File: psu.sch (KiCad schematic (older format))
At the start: 1 part

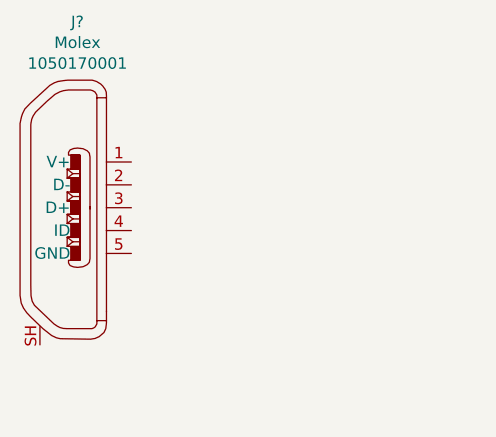
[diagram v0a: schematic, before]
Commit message: Add ESD protection to USB
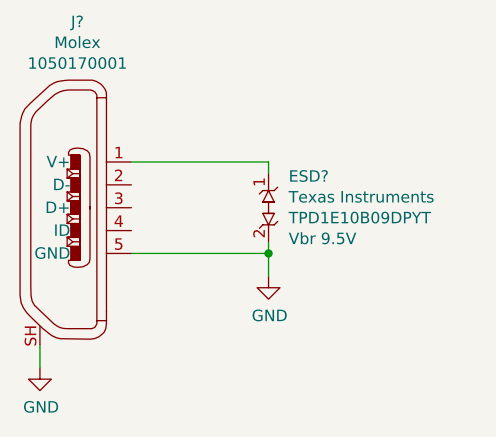
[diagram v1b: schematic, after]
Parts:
- added ESD?: TI-TPD1E10B09DPYT, footprints:TI-TPD1E10B09DPYT_DIODFN2_100X60X45L25X50N, symbol gz_TVS-Diodes:TI-TPD1E10B09DPYT
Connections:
- net at J?.1 (V+): now also ESD?.1
- net GND: now reaches J?.5 (GND)
- net GND: now also J?.SH, ESD?.2
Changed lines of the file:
@@
 	1    0    0    -1
 $EndComp
+$Comp
+L gz_TVS-Diodes:TI-TPD1E10B09DPYT ESD?
+U 1 1 60436474
+P 2350 1900
+F 0 "ESD?" H 2438 2037 50  0000 L CNN
+F 1 "TI-TPD1E10B09DPYT" H 3150 2900 50  0001 L CNN
+F 2 "footprints:TI-TPD1E10B09DPYT_DIODFN2_100X60X45L25X50N" H 3150 2800 50  0001 L CNN
+F 3 "${DATASHEETS}/TI-TPD1E10B09DPYT.pdf" H 2550 2200 50  0001 L CNN
+F 4 "Digikey" H 3150 2700 50  0001 L CNN "Vendor"
+F 5 "296-46461-1-ND" H 3550 2700 50  0001 L CNN "Vendor_PN"
+F 6 "Texas Instruments" H 2438 1946 50  0000 L CNN "Manufacturer"
+F 7 "TPD1E10B09DPYT" H 2438 1855 50  0000 L CNN "MPN"
+F 8 "Circuit protection" H 3150 2600 50  0001 L CNN "Category"
+F 9 "TVS - Diodes" H 3150 2500 50  0001 L CNN "Family"
+F 10 "Y" H 2800 2050 50  0001 L CNN "Fit"
+F 11 "Vbr 9.5V" H 2438 1764 50  0000 L CNN "Breakdown Voltage"
+F 12 "EIA0402" H 3150 2400 50  0001 L CNN "Package"
+	1    2350 1900
+	1    0    0    -1
+$EndComp
+Wire Wire Line
+	1750 1700 2350 1700
+Wire Wire Line
+	2350 1700 2350 1750
+Wire Wire Line
+	2350 2050 2350 2100
+$Comp
+L gz_Power-Symbols:GND #PWR?
+U 1 1 60439CF7
+P 2350 2200
+F 0 "#PWR?" H 2350 1950 50  0001 C CNN
+F 1 "GND" H 2355 2027 50  0000 C CNN
+F 2 "" H 2350 2200 50  0001 C CNN
+F 3 "" H 2350 2200 50  0001 C CNN
+	1    2350 2200
+	1    0    0    -1
+$EndComp
+Wire Wire Line
+	1750 2100 2350 2100
+Connection ~ 2350 2100
+Wire Wire Line
+	2350 2100 2350 2200
+$Comp
+L gz_Power-Symbols:GND #PWR?
+U 1 1 6043BB02
+P 1350 2600
+F 0 "#PWR?" H 1350 2350 50  0001 C CNN
+F 1 "GND" H 1355 2427 50  0000 C CNN
+F 2 "" H 1350 2600 50  0001 C CNN
+F 3 "" H 1350 2600 50  0001 C CNN
+	1    1350 2600
+	1    0    0    -1
+$EndComp
+Wire Wire Line
+	1350 2600 1350 2500
 $EndSCHEMATC

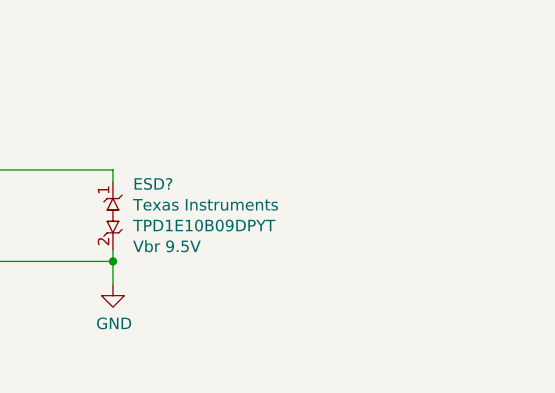
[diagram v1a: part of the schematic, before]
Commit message: Add FB to power input
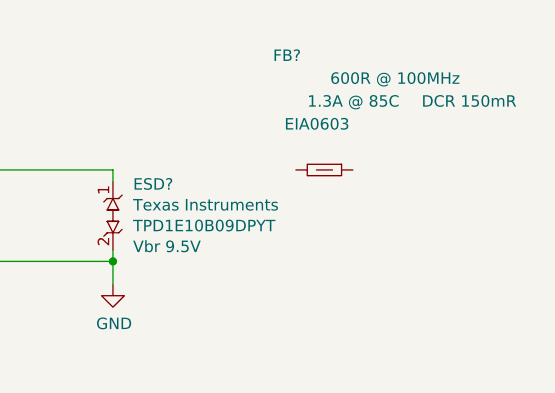
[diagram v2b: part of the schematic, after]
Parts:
- added FB?: FB-EIA0603, footprints_generic:BEADC160X80X95L40N, symbol gz_Ferrite-Beads-and-Chips:FB-EIA0603
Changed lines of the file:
@@
 Wire Wire Line
 	1350 2600 1350 2500
+$Comp
+L gz_Ferrite-Beads-and-Chips:FB-EIA0603 FB?
+U 1 1 6043F2AE
+P 3250 1700
+F 0 "FB?" H 3050 2200 50  0000 L CNN
+F 1 "FB-EIA0603" H 3850 3100 50  0001 L CNN
+F 2 "footprints_generic:BEADC160X80X95L40N" H 3850 3000 50  0001 L CNN
+F 3 "https://ds.murata.co.jp/simsurfing/blm.html?lcid=en-us" H -50 6150 50  0001 L CNN
+F 4 "490-5258-1-ND" H 3850 2900 50  0001 L CNN "Digi-Key_PN"
+F 5 "Murata Electronics" H 3850 2800 50  0001 L CNN "Manufacturer"
+F 6 "BLM18KG601SN1D" H 3850 2700 50  0001 L CNN "MPN"
+F 7 "Filters" H 3850 2600 50  0001 L CNN "Category"
+F 8 "Ferrite Beads and Chips" H 3850 2500 50  0001 L CNN "Family"
+F 9 "600R @ 100MHz" H 3300 2100 50  0000 L CNN "Impedance"
+F 10 "1.3A @ 85C" H 3200 2000 50  0000 L CNN "Current"
+F 11 "DCR 150mR" H 3700 2000 50  0000 L CNN "DCR"
+F 12 "EIA0603" H 3100 1900 50  0000 L CNN "Package"
+	1    3250 1700
+	1    0    0    -1
+$EndComp
 $EndSCHEMATC

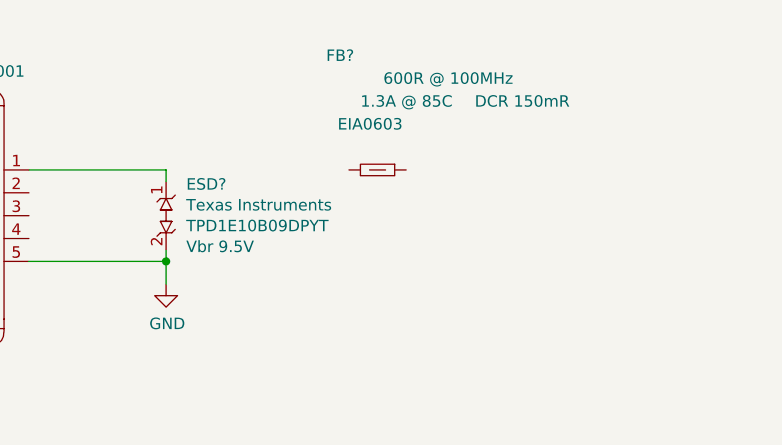
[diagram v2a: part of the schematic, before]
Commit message: Add e-cap on power rail
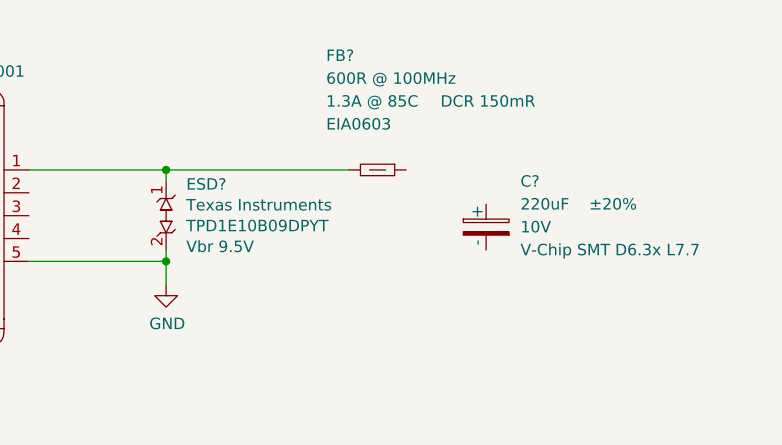
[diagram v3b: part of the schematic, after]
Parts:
- added C?: WE-865080245009, footprints_generic:WE-86508xx450xx_CAPAE660X770D730L255X65N, symbol gz_Aluminum-Electrolytic-Capacitors:WE-865080245009
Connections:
- net at ESD?.1, J?.1 (V+): now also FB?.1
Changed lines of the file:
@@
 F 7 "Filters" H 3850 2600 50  0001 L CNN "Category"
 F 8 "Ferrite Beads and Chips" H 3850 2500 50  0001 L CNN "Family"
-F 9 "600R @ 100MHz" H 3300 2100 50  0000 L CNN "Impedance"
-F 10 "1.3A @ 85C" H 3200 2000 50  0000 L CNN "Current"
-F 11 "DCR 150mR" H 3700 2000 50  0000 L CNN "DCR"
-F 12 "EIA0603" H 3100 1900 50  0000 L CNN "Package"
+F 9 "600R @ 100MHz" H 3050 2100 50  0000 L CNN "Impedance"
+F 10 "1.3A @ 85C" H 3050 2000 50  0000 L CNN "Current"
+F 11 "DCR 150mR" H 3550 2000 50  0000 L CNN "DCR"
+F 12 "EIA0603" H 3050 1900 50  0000 L CNN "Package"
 	1    3250 1700
 	1    0    0    -1
 $EndComp
+Wire Wire Line
+	2350 1700 3150 1700
+Connection ~ 2350 1700
+$Comp
+L gz_Aluminum-Electrolytic-Capacitors:WE-865080245009 C?
+U 1 1 60444CF8
+P 3750 1950
+F 0 "C?" H 3900 2150 50  0000 L CNN
+F 1 "WE-865080245009" H 4650 3550 50  0001 L CNN
+F 2 "footprints_generic:WE-86508xx450xx_CAPAE660X770D730L255X65N" H 4650 3450 50  0001 L CNN
+F 3 "${DATASHEETS}/WE-865080245009.pdf" H 4650 3250 50  0001 L CNN
+F 4 "732-8492-1-ND" H 4650 3350 50  0001 L CNN "Digi-Key_PN"
+F 5 "Würth Elektronik" H 4650 3250 50  0001 L CNN "Manufacturer"
+F 6 "865080245009" H 4650 3150 50  0001 L CNN "MPN"
+F 7 "Capacitors" H 4650 3050 50  0001 L CNN "Category"
+F 8 "Aluminum Electrolytic Capacitors" H 4650 2950 50  0001 L CNN "Family"
+F 9 "220uF" H 3900 2050 50  0000 L CNN "Capacitance"
+F 10 "±20%" H 4200 2050 50  0000 L CNN "Tolerance"
+F 11 "10V" H 3900 1950 50  0000 L CNN "Voltage"
+F 12 "ESR" H 4150 2150 50  0001 L CNN "ESR"
+F 13 "V-Chip SMT D6.3x L7.7" H 3900 1850 50  0000 L CNN "Package"
+	1    3750 1950
+	1    0    0    -1
+$EndComp

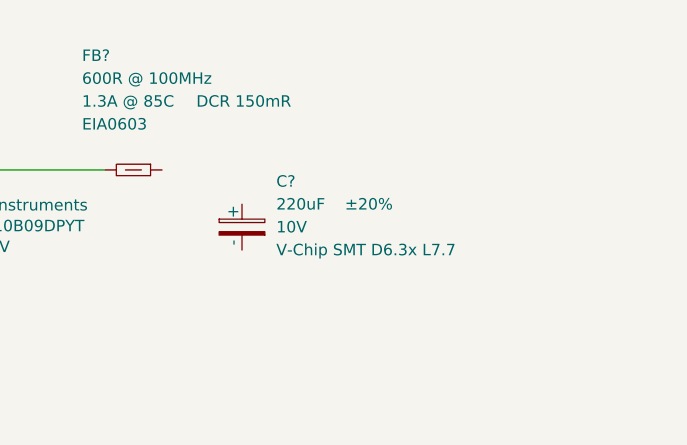
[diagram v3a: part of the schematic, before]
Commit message: Add 1uF cap to power rail
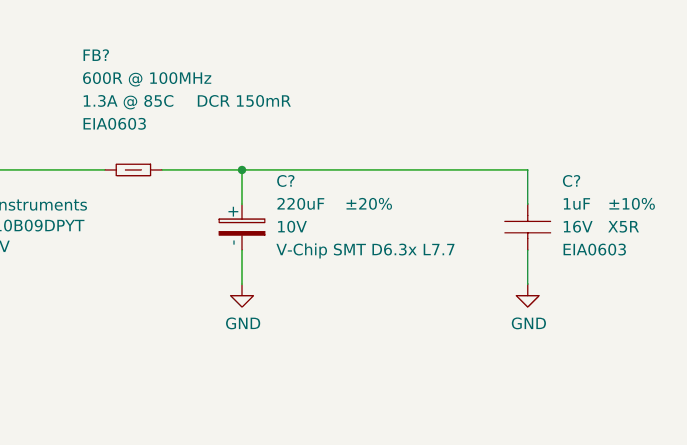
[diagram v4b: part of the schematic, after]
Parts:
- added C?: CAP-EIA0603, footprints_generic:CAPC160X80X95L35N, symbol gz_Ceramic-Capacitors:CAP-EIA0603
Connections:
- net GND: now also C?.2 (-), C?.2
- net at FB?.2: now also C?.1 (+), C?.1
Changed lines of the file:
@@
+	1    0    0    -1
+$EndComp
+$Comp
+L gz_Ceramic-Capacitors:CAP-EIA0603 C?
+U 1 1 6044A8A6
+P 5000 1950
+F 0 "C?" V 4800 2100 50  0000 L CNN
+F 1 "CAP-EIA0603" H 5400 3050 50  0001 L CNN
+F 2 "footprints_generic:CAPC160X80X95L35N" H 1700 6300 50  0001 L CNN
+F 3 "https://api.kemet.com/component-edge/download/specsheet/C0603C105K4PAC7411.pdf" H 1700 6400 50  0001 L CNN
+F 4 "399-C0603C105K4PAC7411CT-ND" H 5400 2950 50  0001 L CNN "Digi-Key_PN"
+F 5 "KEMET" H 5400 2850 50  0001 L CNN "Manufacturer"
+F 6 "C0603C105K4PAC7411" H 5400 2750 50  0001 L CNN "MPN"
+F 7 "Capacitors" H 1700 6700 50  0001 L CNN "Category"
+F 8 "Ceramic Capacitors" H 1700 6800 50  0001 L CNN "Family"
+F 9 "1uF" V 4900 2100 50  0000 L CNN "Capacitance"
+F 10 "±10%" V 4900 2300 50  0000 L CNN "Tolerance"
+F 11 "16V" V 5000 2100 50  0000 L CNN "Voltage"
+F 12 "X5R" V 5000 2300 50  0000 L CNN "Dielectric"
+F 13 "EIA0603" V 5100 2100 50  0000 L CNN "Package"
+	1    5000 1950
+	0    1    1    0
+$EndComp
+Wire Wire Line
+	3400 1700 3750 1700
+Wire Wire Line
+	3750 1700 3750 1850
+Wire Wire Line
+	3750 1700 5000 1700
+Wire Wire Line
+	5000 1700 5000 1850
+Connection ~ 3750 1700
+Wire Wire Line
+	5000 2050 5000 2200
+Wire Wire Line
+	3750 2050 3750 2200
+$Comp
+L gz_Power-Symbols:GND #PWR?
+U 1 1 6044FC52
+P 3750 2200
+F 0 "#PWR?" H 3750 1950 50  0001 C CNN
+F 1 "GND" H 3755 2027 50  0000 C CNN
+F 2 "" H 3750 2200 50  0001 C CNN
+F 3 "" H 3750 2200 50  0001 C CNN
+	1    3750 2200
+	1    0    0    -1
+$EndComp
+$Comp
+L gz_Power-Symbols:GND #PWR?
+U 1 1 60450196
+P 5000 2200
+F 0 "#PWR?" H 5000 1950 50  0001 C CNN
+F 1 "GND" H 5005 2027 50  0000 C CNN
+F 2 "" H 5000 2200 50  0001 C CNN
+F 3 "" H 5000 2200 50  0001 C CNN
+	1    5000 2200
 	1    0    0    -1
 $EndComp

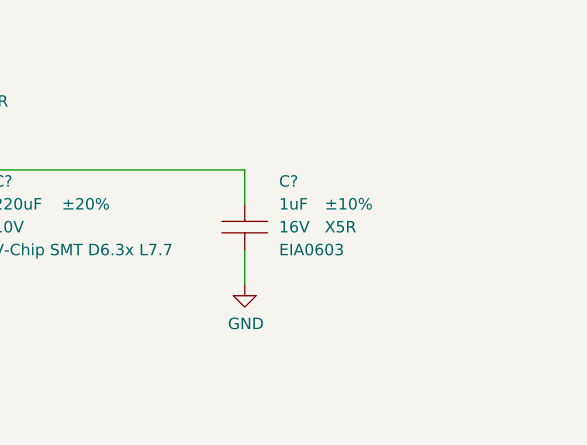
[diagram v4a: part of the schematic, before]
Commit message: Add 0.1uF cap to power rail
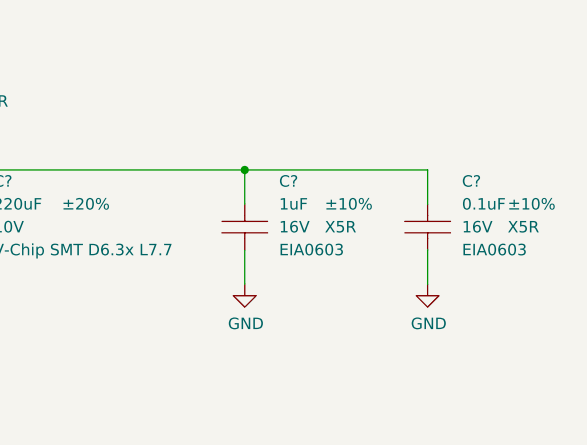
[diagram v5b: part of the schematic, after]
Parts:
- added C?: CAP-EIA0603, footprints_generic:CAPC160X80X95L35N, symbol gz_Ceramic-Capacitors:CAP-EIA0603
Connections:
- net GND: now also C?.2
- net at C?.1, C?.1 (+), FB?.2: now also C?.1
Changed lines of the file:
@@
 	1    0    0    -1
 $EndComp
+$Comp
+L gz_Ceramic-Capacitors:CAP-EIA0603 C?
+U 1 1 60451C07
+P 5800 1950
+F 0 "C?" V 5600 2100 50  0000 L CNN
+F 1 "CAP-EIA0603" H 6200 3050 50  0001 L CNN
+F 2 "footprints_generic:CAPC160X80X95L35N" H 2500 6300 50  0001 L CNN
+F 3 "https://api.kemet.com/component-edge/download/datasheet/C0603C104K4PAC7867.pdf" H 2500 6400 50  0001 L CNN
+F 4 "399-14941-1-ND" H 6200 2950 50  0001 L CNN "Digi-Key_PN"
+F 5 "KEMET" H 6200 2850 50  0001 L CNN "Manufacturer"
+F 6 "C0603C104K4PAC7867" H 6200 2750 50  0001 L CNN "MPN"
+F 7 "Capacitors" H 2500 6700 50  0001 L CNN "Category"
+F 8 "Ceramic Capacitors" H 2500 6800 50  0001 L CNN "Family"
+F 9 "0.1uF" V 5700 2100 50  0000 L CNN "Capacitance"
+F 10 "±10%" V 5700 2300 50  0000 L CNN "Tolerance"
+F 11 "16V" V 5800 2100 50  0000 L CNN "Voltage"
+F 12 "X5R" V 5800 2300 50  0000 L CNN "Dielectric"
+F 13 "EIA0603" V 5900 2100 50  0000 L CNN "Package"
+	1    5800 1950
+	0    1    1    0
+$EndComp
+$Comp
+L gz_Power-Symbols:GND #PWR?
+U 1 1 604524F7
+P 5800 2200
+F 0 "#PWR?" H 5800 1950 50  0001 C CNN
+F 1 "GND" H 5805 2027 50  0000 C CNN
+F 2 "" H 5800 2200 50  0001 C CNN
+F 3 "" H 5800 2200 50  0001 C CNN
+	1    5800 2200
+	1    0    0    -1
+$EndComp
+Wire Wire Line
+	5000 1700 5800 1700
+Wire Wire Line
+	5800 1700 5800 1850
+Connection ~ 5000 1700
+Wire Wire Line
+	5800 2050 5800 2200
 $EndSCHEMATC

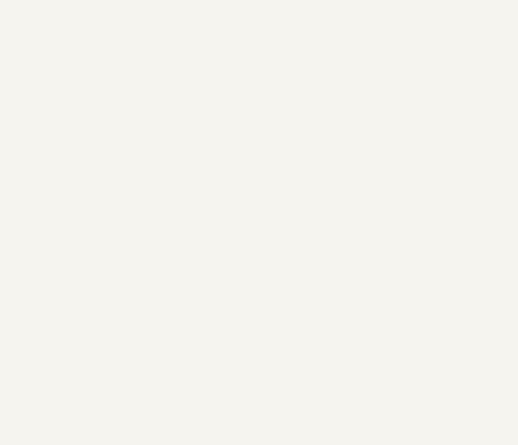
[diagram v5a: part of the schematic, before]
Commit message: Add TI-TLV75533PDBVR.
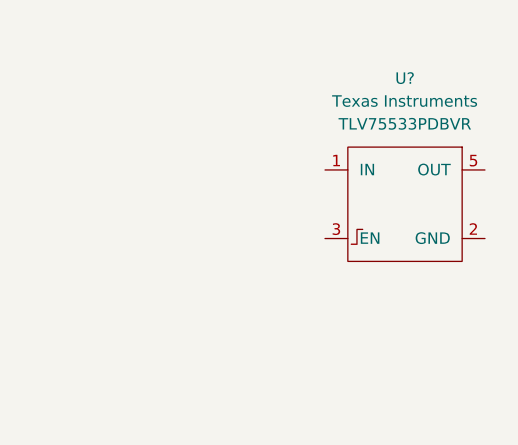
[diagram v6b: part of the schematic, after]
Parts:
- added U?: TI-TLV75533PDBVR, footprints:TI-TLV755_SOT23-5P95_280X145L45X40N, symbol gz_PMIC-Voltage-Regulators-Linear:TI-TLV75533PDBVR
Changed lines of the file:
@@
 Wire Wire Line
 	5800 2050 5800 2200
+$Comp
+L gz_PMIC-Voltage-Regulators-Linear:TI-TLV75533PDBVR U?
+U 1 1 60454D63
+P 8450 1950
+F 0 "U?" H 8400 2600 50  0000 C CNN
+F 1 "TI-TLV75533PDBVR" H 9200 3100 50  0001 L CNN
+F 2 "footprints:TI-TLV755_SOT23-5P95_280X145L45X40N" H 9200 3000 50  0001 L CNN
+F 3 "${DATASHEETS}/TI-TLV755P.pdf" H 8800 2250 50  0001 L CNN
+F 4 "296-50411-1-ND" H 9200 2900 50  0001 L CNN "Digi-Key_PN"
+F 5 "Texas Instruments" H 8400 2500 50  0000 C CNN "Manufacturer"
+F 6 "TLV75533PDBVR" H 8400 2400 50  0000 C CNN "MPN"
+F 7 "Integrated Circuits (ICs)" H 9200 2800 50  0001 L CNN "Category"
+F 8 "PMIC - Voltage Regulators - Linear" H 9200 2700 50  0001 L CNN "Family"
+	1    8450 1950
+	1    0    0    -1
+$EndComp
 $EndSCHEMATC

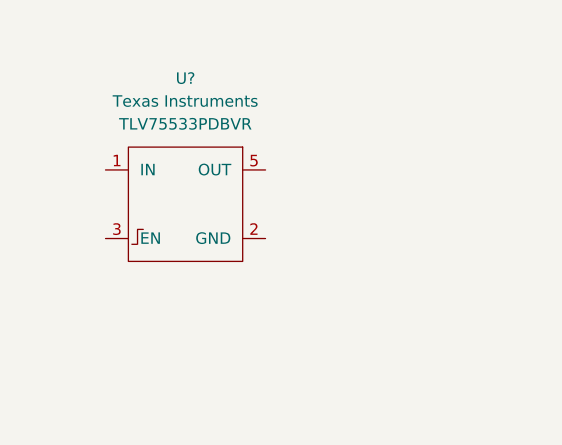
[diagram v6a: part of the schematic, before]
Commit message: Add LDO output cap.
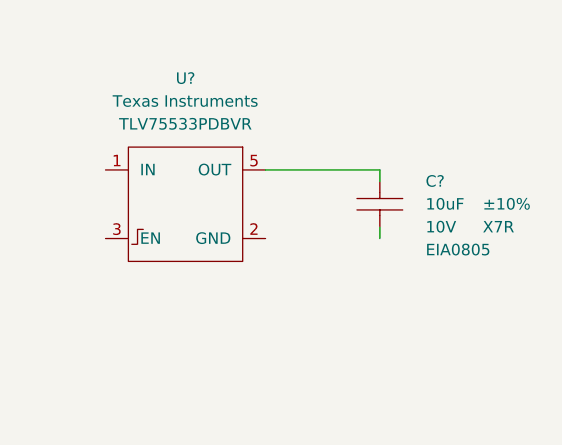
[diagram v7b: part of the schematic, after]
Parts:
- added C?: CAP-EIA0805, footprints_generic:CAPC200X125X110L50N, symbol gz_Ceramic-Capacitors:CAP-EIA0805
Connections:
- wire segments 16 -> 19
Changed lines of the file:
@@
 	1    0    0    -1
 $EndComp
+$Comp
+L gz_Ceramic-Capacitors:CAP-EIA0805 C?
+U 1 1 6046210B
+P 9250 1850
+F 0 "C?" V 9150 2050 50  0000 L CNN
+F 1 "CAP-EIA0805" H 9650 2950 50  0001 L CNN
+F 2 "footprints_generic:CAPC200X125X110L50N" H 5950 6200 50  0001 L CNN
+F 3 "https://www.kemet.com/specsheet/C0805C106K8RACTU" H 5950 6300 50  0001 L CNN
+F 4 "399-7411-1-ND" H 9650 2850 50  0001 L CNN "Digi-Key_PN"
+F 5 "KEMET" H 9650 2750 50  0001 L CNN "Manufacturer"
+F 6 "C0805C106K8RACTU" H 9650 2650 50  0001 L CNN "MPN"
+F 7 "Capacitors" H 5950 6600 50  0001 L CNN "Category"
+F 8 "Ceramic Capacitors" H 5950 6700 50  0001 L CNN "Family"
+F 9 "10uF" V 9250 2050 50  0000 L CNN "Capacitance"
+F 10 "±10%" V 9250 2300 50  0000 L CNN "Tolerance"
+F 11 "10V" V 9350 2050 50  0000 L CNN "Voltage"
+F 12 "X7R" V 9350 2300 50  0000 L CNN "Dielectric"
+F 13 "EIA0805" V 9450 2050 50  0000 L CNN "Package"
+	1    9250 1850
+	0    1    1    0
+$EndComp
+Wire Wire Line
+	8750 1700 9250 1700
+Wire Wire Line
+	9250 1700 9250 1750
+Wire Wire Line
+	9250 1950 9250 2000
 $EndSCHEMATC
